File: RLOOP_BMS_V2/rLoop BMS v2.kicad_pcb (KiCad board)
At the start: 2 copper layers, 78 x 133 mm, 301 parts, among them J1 1241050-7, J2 2-640387-0, Q1 VOS618A-2X001T, Q10 PMV20ENR, Q11 PMV20ENR, Q12 PMV20ENR, Q13 PMV20ENR, Q14 PMV20ENR, Q15 PMV20ENR, Q16 PMV20ENR, Q17 PMV20ENR, Q18 PMV20ENR, Q19 PMV20ENR, Q2 PMV20ENR, Q3 PMV20ENR, Q4 PMV20ENR, Q5 PMV20ENR, Q6 PMV20ENR, Q7 PMV20ENR, Q8 PMV20ENR, Q9 PMV20ENR, U1 bq76PL536A_HTQFP, U2 bq76PL536A_HTQFP, U3 bq76PL536A_HTQFP, U4 MIC5282-5.0YMM, U5 VOS618A-2X001T

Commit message: more WIP
TODO:
Fix pin 50
ground planes
figure out GND_2 weirdness
fix optoisolator 3d model
bq IC 3d model
triple check everything
BOM
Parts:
- added C66: 3.3 nF / 50V/ 10% / SMD 0603, Capacitors_SMD:C_0603, B.Cu at (65.8, 123.3)
- added C67: 33 pF / 50V/ 10% / SMD 0603, Capacitors_SMD:C_0603, B.Cu at (55.5, 133.2)
- added C68: 33 pF / 50V/ 10% / SMD 0603, Capacitors_SMD:C_0603, B.Cu at (53.4, 130.8)
- added C69: 33 pF / 50V/ 10% / SMD 0603, Capacitors_SMD:C_0603, B.Cu at (57.0, 134.3)
- added C70: 3.3 nF / 50V/ 10% / SMD 0603, Capacitors_SMD:C_0603, B.Cu at (62.4, 82.0)
- added C71: 33 pF / 50V/ 10% / SMD 0603, Capacitors_SMD:C_0603, B.Cu at (56.0, 96.0)
- added C72: 33 pF / 50V/ 10% / SMD 0603, Capacitors_SMD:C_0603, B.Cu at (56.0, 94.0)
- added C73: 33 pF / 50V/ 10% / SMD 0603, Capacitors_SMD:C_0603, B.Cu at (54.6, 92.8)
- added C74: 33 pF / 50V/ 10% / SMD 0603, Capacitors_SMD:C_0603, F.Cu at (58.3, 124.2)
- added C75: 33 pF / 50V/ 10% / SMD 0603, Capacitors_SMD:C_0603, F.Cu at (56.9, 124.2)
- added C76: 33 pF / 50V/ 10% / SMD 0603, Capacitors_SMD:C_0603, B.Cu at (56.2, 72.2)
- added C77: 33 pF / 50V/ 10% / SMD 0603, Capacitors_SMD:C_0603, B.Cu at (56.2, 70.9)
- moved R109 3.36 mm to (54.6, 68.6), turned to 0 degrees
- moved C58 1.24 mm to (62.0, 131.5)
- moved R112 1.24 mm to (62.8, 133.7)
- moved R113 1.23 mm to (62.8, 135.2)
- moved TH1 1.19 mm to (63.5, 131.5)
- moved Q1 1.10 mm to (64.5, 164.8)
- moved C63 0.80 mm to (65.5, 77.7)
- moved TH6 0.65 mm to (64.0, 77.6)
- moved R122 0.45 mm to (64.8, 75.5)
- moved R124 0.45 mm to (67.5, 164.6)
- moved R123 0.25 mm to (64.8, 74.0)
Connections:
- C17 pad 2: VDDHV_1 -> GND_2
- C30 pad 1: VDDHV_1 -> GND_2
- C52 pad 1: VDDHV_1 -> GND_2
- D24 pad 2: VDDHV_1 -> GND_2
- D30 pad 2: VDDHV_1 -> GND_2
- D49 pad 1: VDDHV_1 -> GND_2
- J2 pad 14: VDDHV_1 -> GND_2
- Q13 pad 2: VDDHV_1 -> GND_2
- R76 pad 1: VDDHV_1 -> GND_2
- R82 pad 2: VDDHV_1 -> GND_2
- R83 pad 1: VDDHV_1 -> GND_2
- R89 pad 1: VDDHV_1 -> GND_2
- U2 pad 13: VDDHV_1 -> GND_2
- U3 pad 63: VDDHV_1 -> GND_2
- U3 pad 64: VDDHV_1 -> GND_2
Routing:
- net GND_2: track 36.6 -> 181.5 mm
- net /MCU Connector/IRQ_TO_PWR_NODE: track 0.00 -> 142.6 mm, vias 0 -> 1
- net Net-(J1-Pad10): track 0.00 -> 133.3 mm, vias 0 -> 1
- net VDDHV_1: track 132.3 -> 0.00 mm
- net Net-(J1-Pad8): track 0.00 -> 129.8 mm, vias 0 -> 1
- net Net-(J1-Pad4): track 0.00 -> 122.5 mm, vias 0 -> 1
- net /CONTROLLER 1/CS_H: track 125.7 -> 139.1 mm
- net /CONTROLLER 2/SDO_N: track 28.6 -> 38.3 mm, vias 0 -> 2
- net 5V_1: track 52.7 -> 60.1 mm
- net /MCU Connector/SCK_FROM_PWR_NODE: track 127.4 -> 133.9 mm
- net GND_1: track 297.2 -> 302.9 mm, vias 18 -> 19
- net /CONTROLLER 1/DRDY_N: track 24.4 -> 29.9 mm, vias 0 -> 1
- net /CONTROLLER 2/DRDY_N: track 27.6 -> 32.6 mm, vias 0 -> 2
- net /MCU Connector/MISO_TO_PWR_NODE: track 126.3 -> 121.9 mm
- net MCU_3V3: track 23.3 -> 19.7 mm
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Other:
- board size 78 x 133 mm -> 79 x 133 mm

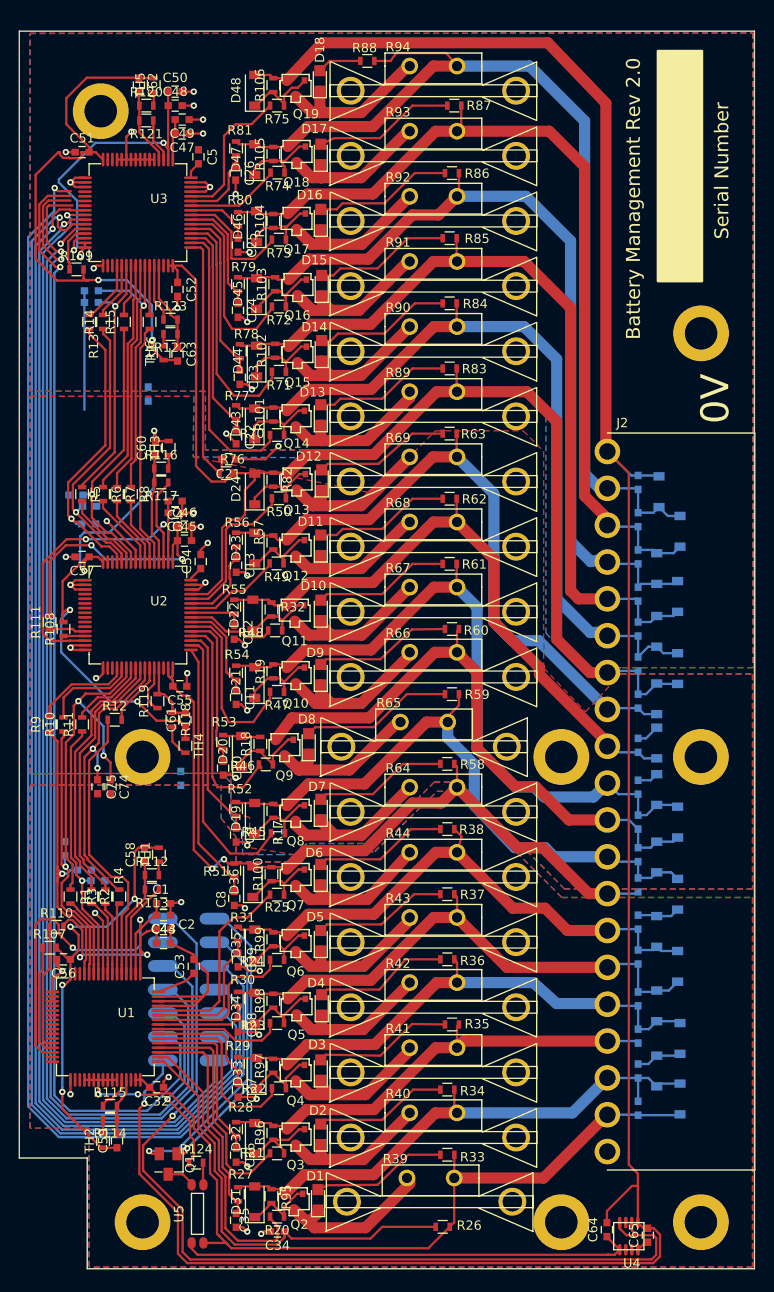
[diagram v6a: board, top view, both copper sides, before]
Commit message: More WIP
Added connector for 1-Wire sensors if we want to put some sensors on the
heat-sinks. Just need to double check everything with the 3d-models.
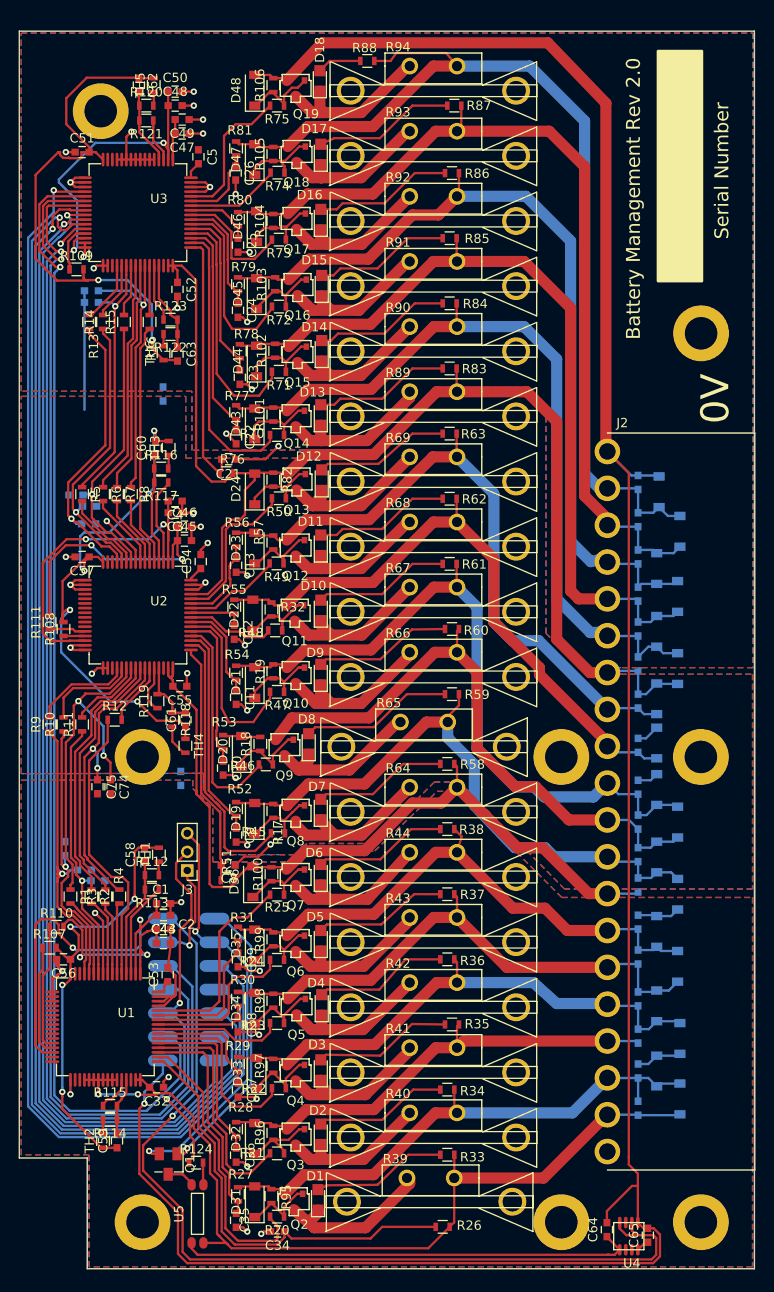
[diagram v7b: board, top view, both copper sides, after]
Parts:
- added J3: TE 2-292161-3, Pin_Headers:Pin_Header_Straight_1x03_Pitch2.00mm, F.Cu at (66.5, 133.2)
- moved C8 3.61 mm to (71.0, 132.7), turned to 0 degrees
- moved C53 2.94 mm to (64.5, 144.4)
- moved C70 1.60 mm to (64.0, 82.0)
- moved R51 1.26 mm to (70.9, 134.2), turned to 180 degrees
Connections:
- J1 pad 10: Net-(J1-Pad10) -> /CONTROLLER 1/FAULT_H
- J1 pad 4: Net-(J1-Pad4) -> /CONTROLLER 1/DRDY_H
- J1 pad 8: Net-(J1-Pad8) -> /CONTROLLER 1/ALERT_H
- J1 pad 9: /MCU Connector/IRQ_TO_PWR_NODE -> /CONTROLLER 1/CONV_H
- U1 pad 50: (no net) -> GND_3
- U2 pad 50: (no net) -> GND_2
- U3 pad 36: Net-(U3-Pad36) -> /CONTROLLER 1/CONV_H
- U3 pad 37: Net-(U3-Pad37) -> /CONTROLLER 1/DRDY_H
- U3 pad 38: Net-(U3-Pad38) -> /CONTROLLER 1/ALERT_H
- U3 pad 39: Net-(U3-Pad39) -> /CONTROLLER 1/FAULT_H
- U3 pad 50: (no net) -> GND_1
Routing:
- net /CONTROLLER 1/CONV_H: track 0.00 -> 143.8 mm, vias 0 -> 1
- net /MCU Connector/IRQ_TO_PWR_NODE: track 142.6 -> 0.00 mm, vias 1 -> 0
- net /CONTROLLER 1/FAULT_H: track 0.00 -> 134.7 mm, vias 0 -> 1
- net Net-(J1-Pad10): track 133.3 -> 0.00 mm, vias 1 -> 0
- net /CONTROLLER 1/ALERT_H: track 0.00 -> 131.7 mm, vias 0 -> 1
- net Net-(J1-Pad8): track 129.8 -> 0.00 mm, vias 1 -> 0
- net /CONTROLLER 1/DRDY_H: track 0.00 -> 123.9 mm, vias 0 -> 1
- net Net-(J1-Pad4): track 122.5 -> 0.00 mm, vias 1 -> 0
- net MCU_3V3: track 19.7 -> 40.0 mm, vias 1 -> 2
- net MCU_GND: track 31.7 -> 45.6 mm, vias 1 -> 2
- net Net-(J1-Pad12): track 0.00 -> 11.6 mm, vias 0 -> 1
- net GND_3: track 142.0 -> 133.4 mm, vias 13 -> 11
- net GND_2: track 181.5 -> 185.4 mm
- net Net-(C53-Pad1): track 4.36 -> 2.00 mm
- net /CONTROLLER 2/MBAT7: track 27.9 -> 26.5 mm

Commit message: more WIP
So close. Need to finish arranging the sild screen and make sure diodes
get put on in the correct orientation.
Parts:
- added REF**: .3MMVia, rLoop_Footprints:.3MMVia, F.Cu at (64.5, 65.8)
- added REF**: .3MMVia, rLoop_Footprints:.3MMVia, F.Cu at (60.6, 64.5)
- added REF**: .3MMVia, rLoop_Footprints:.3MMVia, F.Cu at (54.5, 148.1)
- added REF**: .3MMVia, rLoop_Footprints:.3MMVia, F.Cu at (61.0, 146.8)
- added REF**: .3MMVia, rLoop_Footprints:.3MMVia, F.Cu at (59.7, 146.8)
- added REF**: .3MMVia, rLoop_Footprints:.3MMVia, F.Cu at (58.4, 146.8)
- added REF**: .3MMVia, rLoop_Footprints:.3MMVia, F.Cu at (57.1, 146.8)
- added REF**: .3MMVia, rLoop_Footprints:.3MMVia, F.Cu at (55.8, 146.8)
- added REF**: .3MMVia, rLoop_Footprints:.3MMVia, F.Cu at (59.3, 64.5)
- added REF**: .3MMVia, rLoop_Footprints:.3MMVia, F.Cu at (58.0, 64.5)
- added REF**: .3MMVia, rLoop_Footprints:.3MMVia, F.Cu at (64.5, 63.1)
- added REF**: .3MMVia, rLoop_Footprints:.3MMVia, F.Cu at (54.5, 146.8)
- added REF**: .3MMVia, rLoop_Footprints:.3MMVia, F.Cu at (58.0, 102.5)
- added REF**: .3MMVia, rLoop_Footprints:.3MMVia, F.Cu at (58.0, 59.2)
- added REF**: .3MMVia, rLoop_Footprints:.3MMVia, F.Cu at (63.2, 63.1)
- added REF**: .3MMVia, rLoop_Footprints:.3MMVia, F.Cu at (61.9, 63.1)
- added REF**: .3MMVia, rLoop_Footprints:.3MMVia, F.Cu at (60.6, 63.1)
- added REF**: .3MMVia, rLoop_Footprints:.3MMVia, F.Cu at (59.3, 63.1)
- added REF**: .3MMVia, rLoop_Footprints:.3MMVia, F.Cu at (58.0, 63.1)
- added REF**: .3MMVia, rLoop_Footprints:.3MMVia, F.Cu at (64.5, 61.9)
- added REF**: .3MMVia, rLoop_Footprints:.3MMVia, F.Cu at (63.2, 65.8)
- added REF**: .3MMVia, rLoop_Footprints:.3MMVia, F.Cu at (63.2, 61.9)
- added REF**: .3MMVia, rLoop_Footprints:.3MMVia, F.Cu at (61.9, 61.9)
- added REF**: .3MMVia, rLoop_Footprints:.3MMVia, F.Cu at (60.6, 61.9)
- added REF**: .3MMVia, rLoop_Footprints:.3MMVia, F.Cu at (59.3, 61.9)
- added REF**: .3MMVia, rLoop_Footprints:.3MMVia, F.Cu at (58.0, 61.9)
- added REF**: .3MMVia, rLoop_Footprints:.3MMVia, F.Cu at (64.5, 60.5)
- added REF**: .3MMVia, rLoop_Footprints:.3MMVia, F.Cu at (63.2, 60.5)
- added REF**: .3MMVia, rLoop_Footprints:.3MMVia, F.Cu at (61.9, 60.5)
- added REF**: .3MMVia, rLoop_Footprints:.3MMVia, F.Cu at (60.6, 60.5)
- added REF**: .3MMVia, rLoop_Footprints:.3MMVia, F.Cu at (59.3, 60.5)
- added REF**: .3MMVia, rLoop_Footprints:.3MMVia, F.Cu at (61.9, 65.8)
- added REF**: .3MMVia, rLoop_Footprints:.3MMVia, F.Cu at (58.0, 60.5)
- added REF**: .3MMVia, rLoop_Footprints:.3MMVia, F.Cu at (64.5, 59.2)
- added REF**: .3MMVia, rLoop_Footprints:.3MMVia, F.Cu at (63.2, 59.2)
- added REF**: .3MMVia, rLoop_Footprints:.3MMVia, F.Cu at (61.9, 59.2)
- added REF**: .3MMVia, rLoop_Footprints:.3MMVia, F.Cu at (60.6, 59.2)
- added REF**: .3MMVia, rLoop_Footprints:.3MMVia, F.Cu at (59.3, 59.2)
- added REF**: .3MMVia, rLoop_Footprints:.3MMVia, F.Cu at (64.5, 109.0)
- added REF**: .3MMVia, rLoop_Footprints:.3MMVia, F.Cu at (63.2, 109.0)
- added REF**: .3MMVia, rLoop_Footprints:.3MMVia, F.Cu at (61.9, 109.0)
- added REF**: .3MMVia, rLoop_Footprints:.3MMVia, F.Cu at (60.6, 109.0)
- added REF**: .3MMVia, rLoop_Footprints:.3MMVia, F.Cu at (60.6, 65.8)
- added REF**: .3MMVia, rLoop_Footprints:.3MMVia, F.Cu at (59.3, 109.0)
- added REF**: .3MMVia, rLoop_Footprints:.3MMVia, F.Cu at (58.0, 109.0)
- added REF**: .3MMVia, rLoop_Footprints:.3MMVia, F.Cu at (64.5, 107.7)
- added REF**: .3MMVia, rLoop_Footprints:.3MMVia, F.Cu at (63.2, 107.7)
- added REF**: .3MMVia, rLoop_Footprints:.3MMVia, F.Cu at (61.9, 107.7)
- added REF**: .3MMVia, rLoop_Footprints:.3MMVia, F.Cu at (60.6, 107.7)
- added REF**: .3MMVia, rLoop_Footprints:.3MMVia, F.Cu at (59.3, 107.7)
- added REF**: .3MMVia, rLoop_Footprints:.3MMVia, F.Cu at (58.0, 107.7)
- added REF**: .3MMVia, rLoop_Footprints:.3MMVia, F.Cu at (64.5, 106.4)
- added REF**: .3MMVia, rLoop_Footprints:.3MMVia, F.Cu at (63.2, 106.4)
- added REF**: .3MMVia, rLoop_Footprints:.3MMVia, F.Cu at (59.3, 65.8)
- added REF**: .3MMVia, rLoop_Footprints:.3MMVia, F.Cu at (61.9, 106.4)
- added REF**: .3MMVia, rLoop_Footprints:.3MMVia, F.Cu at (60.6, 106.4)
- added REF**: .3MMVia, rLoop_Footprints:.3MMVia, F.Cu at (59.3, 106.4)
- added REF**: .3MMVia, rLoop_Footprints:.3MMVia, F.Cu at (58.0, 106.4)
- added REF**: .3MMVia, rLoop_Footprints:.3MMVia, F.Cu at (64.5, 105.1)
- added REF**: .3MMVia, rLoop_Footprints:.3MMVia, F.Cu at (63.2, 105.1)
- added REF**: .3MMVia, rLoop_Footprints:.3MMVia, F.Cu at (61.9, 105.1)
- added REF**: .3MMVia, rLoop_Footprints:.3MMVia, F.Cu at (60.6, 105.1)
- added REF**: .3MMVia, rLoop_Footprints:.3MMVia, F.Cu at (59.3, 105.1)
- added REF**: .3MMVia, rLoop_Footprints:.3MMVia, F.Cu at (58.0, 105.1)
- added REF**: .3MMVia, rLoop_Footprints:.3MMVia, F.Cu at (58.0, 65.8)
- added REF**: .3MMVia, rLoop_Footprints:.3MMVia, F.Cu at (64.5, 103.8)
- added REF**: .3MMVia, rLoop_Footprints:.3MMVia, F.Cu at (63.2, 103.8)
- added REF**: .3MMVia, rLoop_Footprints:.3MMVia, F.Cu at (61.9, 103.8)
- added REF**: .3MMVia, rLoop_Footprints:.3MMVia, F.Cu at (60.6, 103.8)
- added REF**: .3MMVia, rLoop_Footprints:.3MMVia, F.Cu at (59.3, 103.8)
- added REF**: .3MMVia, rLoop_Footprints:.3MMVia, F.Cu at (58.0, 103.8)
- added REF**: .3MMVia, rLoop_Footprints:.3MMVia, F.Cu at (64.5, 102.5)
- added REF**: .3MMVia, rLoop_Footprints:.3MMVia, F.Cu at (63.2, 102.5)
- added REF**: .3MMVia, rLoop_Footprints:.3MMVia, F.Cu at (61.9, 102.5)
- added REF**: .3MMVia, rLoop_Footprints:.3MMVia, F.Cu at (60.6, 102.5)
- added REF**: .3MMVia, rLoop_Footprints:.3MMVia, F.Cu at (64.5, 64.5)
- added REF**: .3MMVia, rLoop_Footprints:.3MMVia, F.Cu at (59.3, 102.5)
- added REF**: .3MMVia, rLoop_Footprints:.3MMVia, F.Cu at (61.0, 153.2)
- added REF**: .3MMVia, rLoop_Footprints:.3MMVia, F.Cu at (59.7, 153.2)
- added REF**: .3MMVia, rLoop_Footprints:.3MMVia, F.Cu at (58.4, 153.2)
- added REF**: .3MMVia, rLoop_Footprints:.3MMVia, F.Cu at (57.1, 153.2)
- added REF**: .3MMVia, rLoop_Footprints:.3MMVia, F.Cu at (55.8, 153.2)
- added REF**: .3MMVia, rLoop_Footprints:.3MMVia, F.Cu at (54.5, 153.2)
- added REF**: .3MMVia, rLoop_Footprints:.3MMVia, F.Cu at (61.0, 151.9)
- added REF**: .3MMVia, rLoop_Footprints:.3MMVia, F.Cu at (59.7, 151.9)
- added REF**: .3MMVia, rLoop_Footprints:.3MMVia, F.Cu at (58.4, 151.9)
- added REF**: .3MMVia, rLoop_Footprints:.3MMVia, F.Cu at (63.2, 64.5)
- added REF**: .3MMVia, rLoop_Footprints:.3MMVia, F.Cu at (57.1, 151.9)
- added REF**: .3MMVia, rLoop_Footprints:.3MMVia, F.Cu at (55.8, 151.9)
- added REF**: .3MMVia, rLoop_Footprints:.3MMVia, F.Cu at (54.5, 151.9)
- added REF**: .3MMVia, rLoop_Footprints:.3MMVia, F.Cu at (61.0, 150.7)
- added REF**: .3MMVia, rLoop_Footprints:.3MMVia, F.Cu at (59.7, 150.7)
- added REF**: .3MMVia, rLoop_Footprints:.3MMVia, F.Cu at (58.4, 150.7)
- added REF**: .3MMVia, rLoop_Footprints:.3MMVia, F.Cu at (57.1, 150.7)
- added REF**: .3MMVia, rLoop_Footprints:.3MMVia, F.Cu at (55.8, 150.7)
- added REF**: .3MMVia, rLoop_Footprints:.3MMVia, F.Cu at (54.5, 150.7)
- added REF**: .3MMVia, rLoop_Footprints:.3MMVia, F.Cu at (61.0, 149.3)
- added REF**: .3MMVia, rLoop_Footprints:.3MMVia, F.Cu at (61.9, 64.5)
- added REF**: .3MMVia, rLoop_Footprints:.3MMVia, F.Cu at (59.7, 149.3)
- added REF**: .3MMVia, rLoop_Footprints:.3MMVia, F.Cu at (58.4, 149.3)
- added REF**: .3MMVia, rLoop_Footprints:.3MMVia, F.Cu at (57.1, 149.3)
- added REF**: .3MMVia, rLoop_Footprints:.3MMVia, F.Cu at (55.8, 149.3)
- added REF**: .3MMVia, rLoop_Footprints:.3MMVia, F.Cu at (54.5, 149.3)
- added REF**: .3MMVia, rLoop_Footprints:.3MMVia, F.Cu at (61.0, 148.1)
- added REF**: .3MMVia, rLoop_Footprints:.3MMVia, F.Cu at (59.7, 148.1)
- added REF**: .3MMVia, rLoop_Footprints:.3MMVia, F.Cu at (58.4, 148.1)
- added REF**: .3MMVia, rLoop_Footprints:.3MMVia, F.Cu at (57.1, 148.1)
- added REF**: .3MMVia, rLoop_Footprints:.3MMVia, F.Cu at (55.8, 148.1)
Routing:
- net GND_1: track 303.2 -> 306.4 mm
- net /DISCHARGE_3/CELL_4: track 55.1 -> 57.3 mm
- net /DISCHARGE_2/CELL_4: track 69.3 -> 71.1 mm
- net /DISCHARGE_2/CELL_2: track 69.3 -> 71.0 mm
- net /DISCHARGE_2/CELL_1: track 74.0 -> 75.5 mm
- net GND_3: track 133.4 -> 134.4 mm
- net Net-(C3-Pad2): track 35.8 -> 34.9 mm
